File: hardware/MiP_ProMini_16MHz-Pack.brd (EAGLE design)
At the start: 41.4 x 63.8 mm, 47 parts, among them Q1 8MHz, U1 ATMEGA328, U2 MIC5205, U3 TS3USB221A

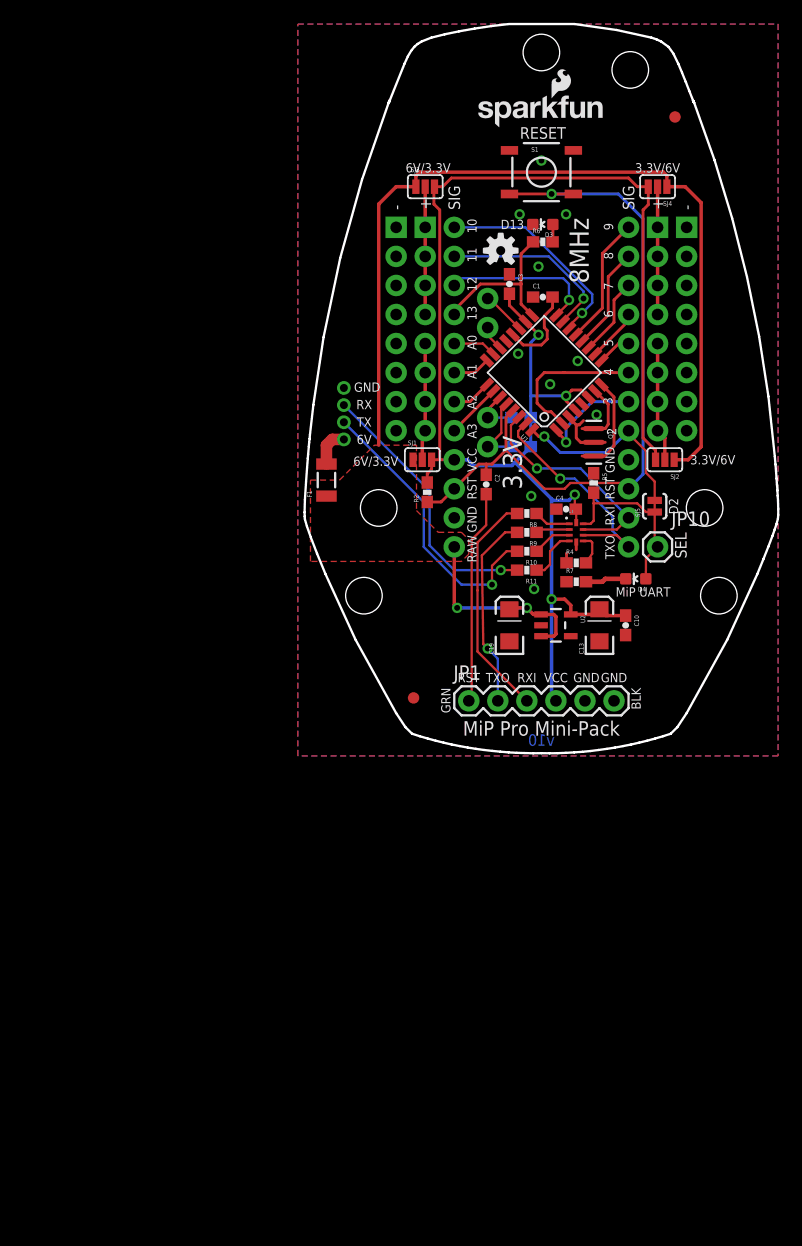
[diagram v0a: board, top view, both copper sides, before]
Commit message: Update schematic to 16MHz / 5V
The ATMEGA328 can't reliably receive data from the MiP at 115200 bps
when running at 8MHz. This commit bumps the clock rate up to 16MHz and
bumps the voltage up to 5V so that the AVR can reliably run at this
higher rate.

Other changes to the schematic include:
* By default the VCC pin of the FTDI header is no longer connected to
  anything. This was done so that the user doesn't risk powering the
  board from both the MiP batteries and the FTDI adapter at the same
  time. It also means that the user doesn't need to worry about whether
  their FTDI adapter is configured to place 5V or 3.3V on this pin. If
  the user wants to power the board from a 5V FTDI cable when MiP
  battery power is disconnected then they can short the two pins of J1.
* The TS3USB221A switch is still powered at 3.3V. I added 1k ohm
  current limiting resistors to its inputs and also added a schottky
  diode for level conversion on the TXO pin.
* Added an AVR ISP header to make it easier to get the Arduino
  bootloader initially loaded into the ATMEGA328. The user would
  want to do this bootloader programming before C2 is installed on the
  RESET line since it will cause the programming to fail otherwise.
* I cascaded the 3.3V regulator off of the 5V supply so that the board
  will work if powered from the FTDI cable.
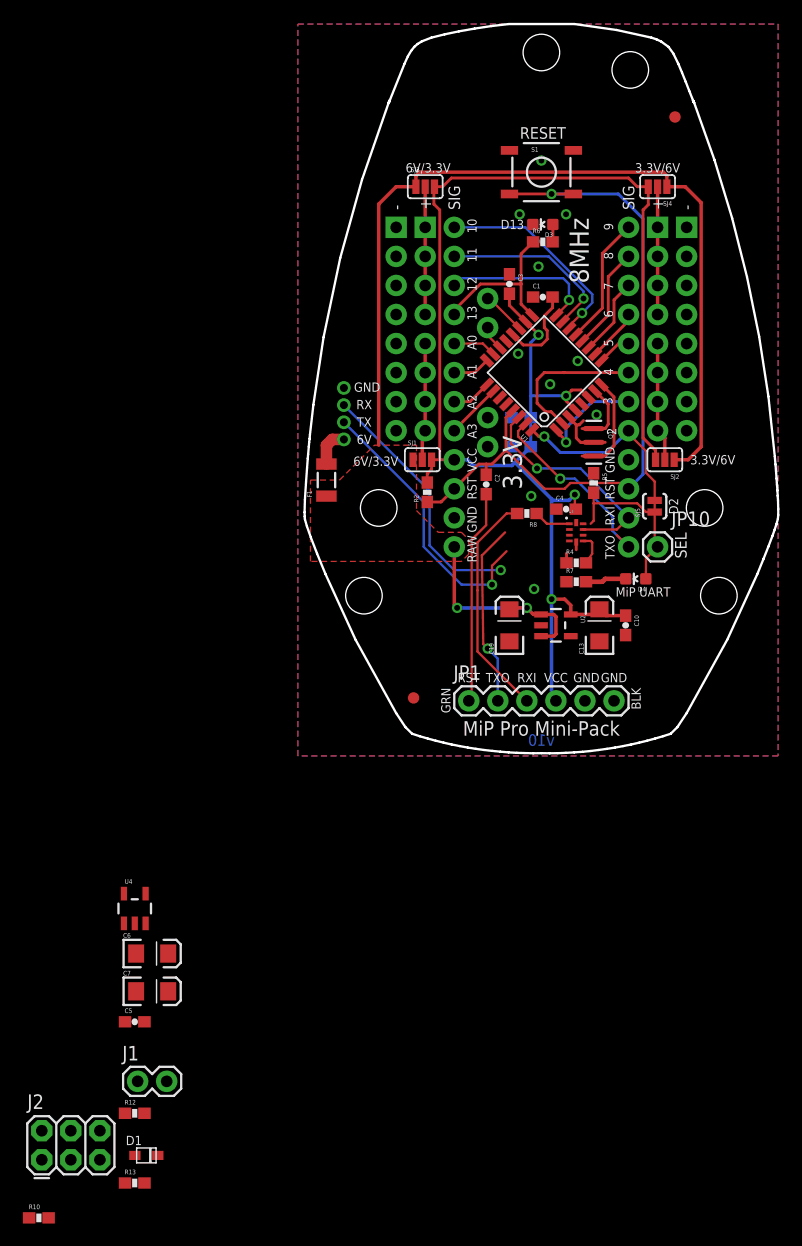
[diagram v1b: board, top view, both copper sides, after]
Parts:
- removed LOGO1: SFE_LOGO_NAME_FLAME.1_INCH, SparkFun-Aesthetics:SFE_LOGO_NAME_FLAME_.1
- removed LOGO2: OSHW-LOGOS, SparkFun-Aesthetics:OSHW-LOGO-S
- removed R11, R9: 1K, SparkFun-Resistors:0603-RES
- added C5: 0.1uF, SparkFun-Capacitors:0603-CAP
- added C6, C7: 10uF, SparkFun:EIA3216
- added D1: ZLLS410TA, adafruit:SOD-323F
- added J1: (no value), SparkFun-Connectors:1X02
- added J2: AVR_ISP, SparkFun-Connectors:2X3
- added R12, R13: 1k, SparkFun-Resistors:0603-RES
- added U4: MIC5205-3.3, SparkFun-PowerIC:SOT23-5
- Q1: value 8MHz -> 16MHZ
- U2: value MIC5205 -> MIC5205-5.0
- moved R10 72.2 mm to (-22.6, -40.4), turned to 0 degrees
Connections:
- removed net N$10: R11.1, U3.4
- removed net N$13: R9.1, U3.2
- removed net VCC: C10.1, C13.A, C3.2, C4.2, JP1.4, JP6.4, R1.2, R2.2, R3.2, SJ1.3, SJ2.3, SJ3.3, SJ4.3, U1.18, U1.4, U1.6, U2.5, U3.10
- new net 3.3V: C4.2, C5.1, C6.A, D1.C, U3.10, U4.5
- new net 5V: C10.1, C13.A, C3.2, C7.A, J1.1, J2.2, JP6.4, R1.2, R2.2, R3.2, SJ1.3, SJ2.3, SJ3.3, SJ4.3, U1.18, U1.4, U1.6, U2.5, U4.1, U4.3
- new net N$15: J1.2, JP1.4
- new net N$16: R12.2, U3.9
- new net N$18: D1.A, R13.2, U3.7
- net GND: now also C5.2, C6.C, C7.C, J2.6, U4.2
- net MISO: now also J2.1
- net MOSI: now also J2.4
- net RESET: now also J2.5
- net SCK: now also J2.3
- net SELECT: now also R12.1; no longer U3.9
- net TXO: now also R13.1; no longer U3.7
- net TXO_MIP: now also U3.4; no longer R11.2
- net TXO_PROG: now also U3.2; no longer R9.2
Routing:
- net VCC: track 136.6 -> 0.00 mm, vias 4 -> 0
- net 5V: track 0.00 -> 134.7 mm, vias 0 -> 4
- net A5: track 6.47 -> 0.00 mm
- net N$10: track 4.59 -> 0.00 mm
- net A4: track 4.26 -> 0.00 mm
- net N$9: track 3.45 -> 0.00 mm
- net N$13: track 2.97 -> 0.00 mm
- net TXO: track 20.2 -> 17.3 mm
- net TXO_MIP: track 23.9 -> 22.5 mm
- net TXO_PROG: track 17.2 -> 16.1 mm
- net RXI_MIP: track 25.5 -> 24.6 mm
- net SELECT: track 15.5 -> 14.9 mm

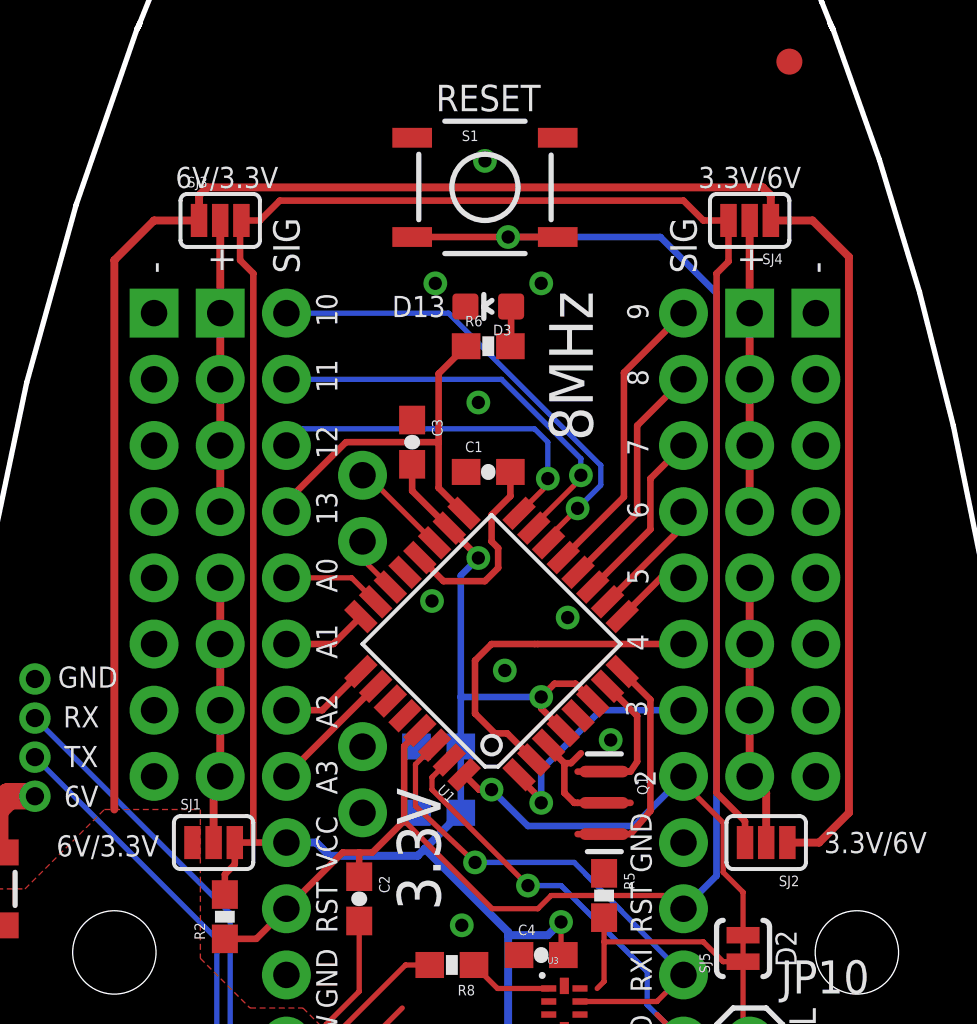
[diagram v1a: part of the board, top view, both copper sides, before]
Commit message: Add 3.3V to headers for v2
Revision 2 of the schematic now allows the lower portion of the
vertical power buses to be selected between 3.3V and 6V while the upper
portion can be selected between 5V and 6V. Previously only the
regulated 5V and unregulated 6V were available for prototyping but it
makes sense to expose the regulated 3.3V as well incase the user wants
to use 3.3V peripherals.
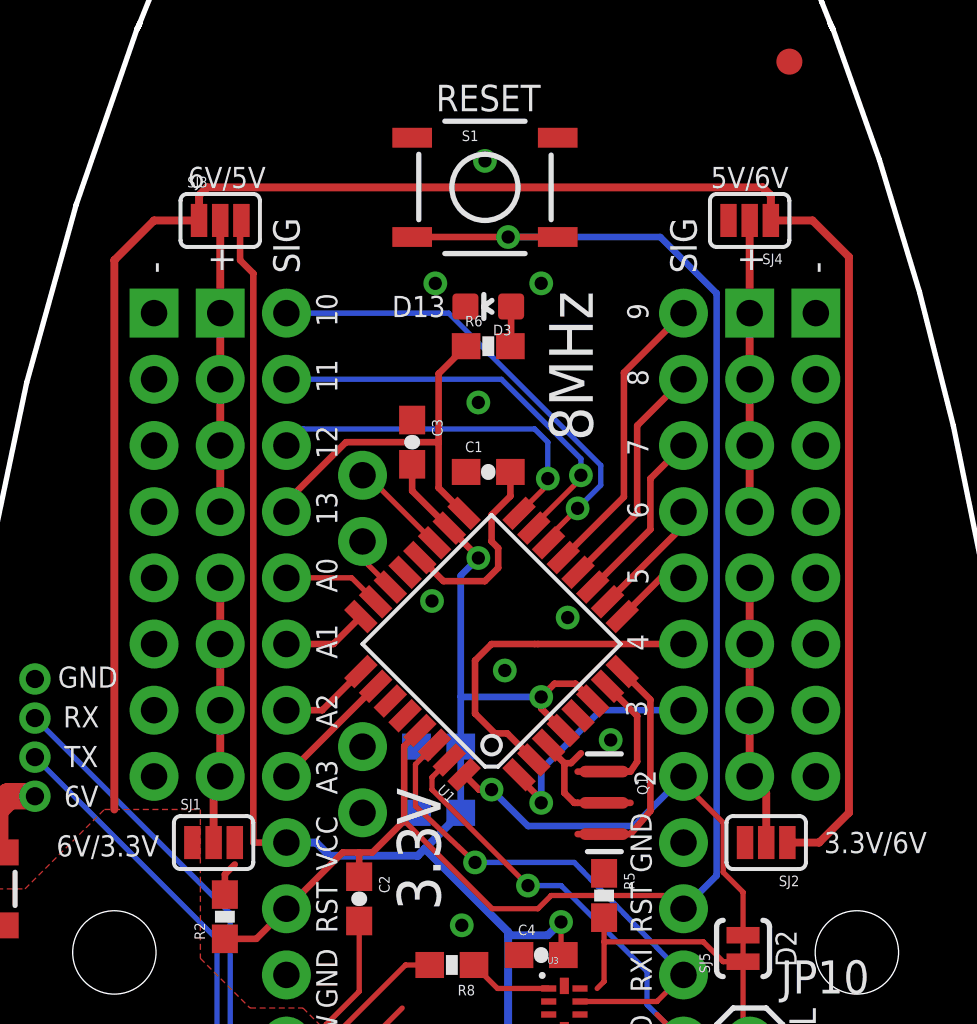
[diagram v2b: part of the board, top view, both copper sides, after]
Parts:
- D4: value GREEN -> Green
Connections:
- net 3.3V: now also SJ3.3, SJ4.3
- net 5V: no longer SJ3.3, SJ4.3
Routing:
- net 5V: track 134.7 -> 89.3 mm
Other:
- board text added: "5V/6V"
- board text added: "6V/5V"
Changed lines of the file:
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@@
 <text x="18.796" y="46.482" size="0.8128" layer="21" font="vector" ratio="15" rot="R180" align="center">D13</text>
 <text x="6.858" y="25.781" size="0.8128" layer="21" font="vector" ratio="15" align="center">6V/3.3V</text>
-<text x="11.43" y="51.435" size="0.8128" layer="21" font="vector" ratio="15" align="center">6V/3.3V</text>
-<text x="31.496" y="51.435" size="0.8128" layer="21" font="vector" ratio="15" align="center">3.3V/6V</text>
+<text x="11.43" y="51.435" size="0.8128" layer="21" font="vector" ratio="15" align="center">6V/5V</text>
+<text x="31.496" y="51.435" size="0.8128" layer="21" font="vector" ratio="15" align="center">5V/6V</text>
 <text x="36.322" y="25.908" size="0.8128" layer="21" font="vector" ratio="15" align="center">3.3V/6V</text>
 <text x="22.606" y="6.858" size="0.8128" layer="21" font="vector" ratio="15" align="center">VCC</text>
@@
 <attribute name="PROD_ID" value="IC-12115" x="21.844" y="27.686" size="1.778" layer="27" display="off"/>
 </element>
-<element name="D4" library="SparkFun-LED" package="LED-0603" value="GREEN" x="29.591" y="15.494" rot="R90">
+<element name="D4" library="SparkFun-LED" package="LED-0603" value="Green" x="29.591" y="15.494" rot="R90">
 <attribute name="PROD_ID" value="DIO-00821" x="32.385" y="7.112" size="1.778" layer="27" rot="R90" display="off"/>
 </element>
@@
 <contactref element="R1" pad="2"/>
 <contactref element="R3" pad="2"/>
-<contactref element="SJ4" pad="3"/>
-<contactref element="SJ2" pad="3"/>
-<wire x1="11.7348" y1="25.908" x2="12.446" y2="25.908" width="0.254" layer="1"/>
 <wire x1="12.446" y1="25.908" x2="13.716" y2="25.908" width="0.254" layer="1"/>
 <wire x1="12.446" y1="47.752" x2="12.446" y2="25.908" width="0.254" layer="1"/>
-<wire x1="30.6832" y1="49.784" x2="30.6832" y2="48.2092" width="0.254" layer="1"/>
-<wire x1="30.6832" y1="48.2092" x2="30.226" y2="47.752" width="0.254" layer="1"/>
 <wire x1="11.938" y1="48.26" x2="12.446" y2="47.752" width="0.254" layer="1"/>
 <wire x1="19.968884375" y1="37.9775375" x2="18.542" y2="39.404428125" width="0.254" layer="1"/>
@@
 <wire x1="23.749" y1="22.352" x2="22.225" y2="22.352" width="0.3048" layer="16"/>
 <wire x1="22.225" y1="5.207" x2="22.225" y2="13.716" width="0.3048" layer="16"/>
-<contactref element="SJ1" pad="3"/>
-<contactref element="SJ3" pad="3"/>
 <wire x1="22.225" y1="13.716" x2="22.225" y2="22.352" width="0.3048" layer="16"/>
 <contactref element="C13" pad="A"/>
@@
 <wire x1="23.368" y1="13.716" x2="22.225" y2="13.716" width="0.3048" layer="1"/>
 <via x="22.225" y="13.716" extent="1-16" drill="0.508"/>
-<wire x1="11.7348" y1="25.908" x2="11.7348" y2="25.0698" width="0.254" layer="1"/>
 <wire x1="11.7348" y1="25.0698" x2="11.3538" y2="24.6888" width="0.254" layer="1"/>
 <wire x1="11.3538" y1="24.6888" x2="11.3538" y2="23.9132" width="0.254" layer="1"/>
-<wire x1="30.226" y1="47.752" x2="30.226" y2="27.813" width="0.254" layer="1"/>
-<wire x1="30.226" y1="27.813" x2="31.3182" y2="26.7208" width="0.254" layer="1"/>
-<wire x1="31.3182" y1="26.7208" x2="31.3182" y2="25.908" width="0.254" layer="1"/>
-<wire x1="11.9888" y1="49.784" x2="12.7" y2="49.784" width="0.254" layer="1"/>
-<wire x1="12.7" y1="49.784" x2="13.462" y2="50.546" width="0.254" layer="1"/>
-<wire x1="13.462" y1="50.546" x2="28.956" y2="50.546" width="0.254" layer="1"/>
-<wire x1="28.956" y1="50.546" x2="29.718" y2="49.784" width="0.254" layer="1"/>
-<wire x1="29.718" y1="49.784" x2="30.6832" y2="49.784" width="0.254" layer="1"/>
 <wire x1="11.938" y1="48.26" x2="11.938" y2="49.784" width="0.254" layer="1"/>
-<wire x1="11.9888" y1="49.784" x2="11.938" y2="49.784" width="0.254" layer="1"/>
 <wire x1="20.408" y1="36.156" x2="21.082" y2="36.83" width="0.254" layer="16"/>
 <wire x1="20.408" y1="29.591" x2="20.408" y2="31.496" width="0.254" layer="16"/>
@@
 <contactref element="J1" pad="1"/>
 <contactref element="J2" pad="2"/>
-<wire x1="-13.97" y1="-28.448" x2="-22.352" y2="-32.766" width="0" layer="19" extent="1-1"/>
-<wire x1="-11.3" y1="-20.574" x2="-13.97" y2="-28.448" width="0" layer="19" extent="1-1"/>
-<wire x1="-13.274" y1="-14.6351" x2="-11.3" y2="-20.574" width="0" layer="19" extent="1-1"/>
+<contactref element="SJ1" pad="3"/>
+<contactref element="SJ2" pad="3"/>
+<wire x1="24.257" y1="22.86" x2="31.3182" y2="25.908" width="0" layer="19" extent="1-1"/>
+<wire x1="11.7348" y1="25.908" x2="12.446" y2="25.908" width="0" layer="19" extent="1-1"/>
+<wire x1="11.7348" y1="25.0698" x2="11.7348" y2="25.908" width="0" layer="19" extent="1-1"/>
+<wire x1="-13.274" y1="-14.6351" x2="22.225" y2="5.207" width="0" layer="19" extent="1-16"/>
 <wire x1="-15.174" y1="-14.6351" x2="-13.274" y2="-14.6351" width="0" layer="19" extent="1-1"/>
-<wire x1="22.225" y1="5.207" x2="-13.274" y2="-14.6351" width="0" layer="19" extent="1-16"/>
+<wire x1="-11.3" y1="-20.574" x2="-13.274" y2="-14.6351" width="0" layer="19" extent="1-1"/>
+<wire x1="-13.97" y1="-28.448" x2="-11.3" y2="-20.574" width="0" layer="19" extent="1-1"/>
+<wire x1="-22.352" y1="-32.766" x2="-13.97" y2="-28.448" width="0" layer="19" extent="1-1"/>
 </signal>
 <signal name="3.3V">
@@
 <contactref element="U3" pad="10"/>
 <contactref element="D1" pad="C"/>
+<contactref element="SJ3" pad="3"/>
+<contactref element="SJ4" pad="3"/>
+<wire x1="11.9888" y1="49.784" x2="30.6832" y2="49.784" width="0" layer="19" extent="1-1"/>
+<wire x1="24.345" y1="21.59" x2="30.6832" y2="49.784" width="0" layer="19" extent="1-1"/>
 <wire x1="24.384" y1="20.408" x2="24.345" y2="21.59" width="0" layer="19" extent="1-1"/>
 <wire x1="-15.174" y1="-12.0349" x2="24.384" y2="20.408" width="0" layer="19" extent="1-1"/>
